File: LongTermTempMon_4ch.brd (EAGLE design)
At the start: 58.4 x 53.3 mm, 26 parts, among them IC2 LTC2418

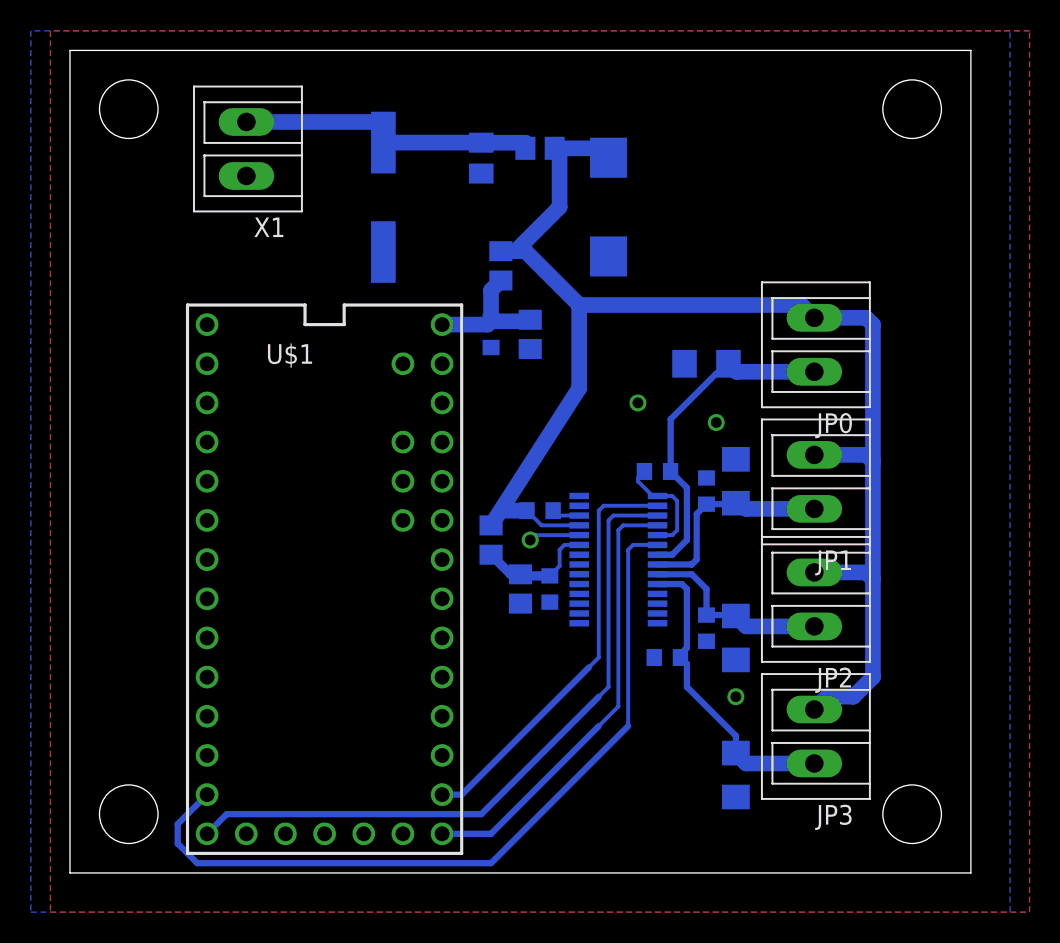
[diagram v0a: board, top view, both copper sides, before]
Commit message: Modified circuit to have reference resistor tied to +5V instead of Gnd
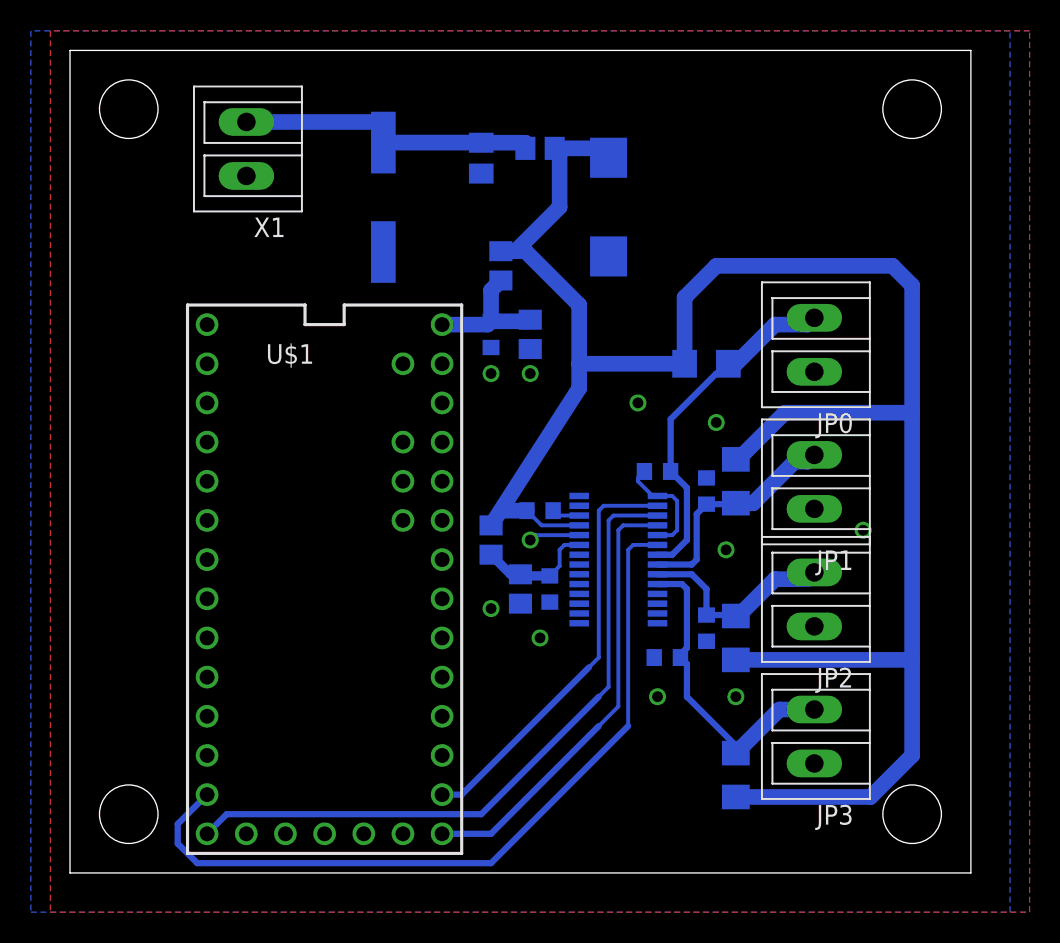
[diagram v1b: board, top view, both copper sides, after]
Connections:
- net GND: now also JP0.1, JP1.1, JP2.1, JP3.1; no longer R0.1, R1.1, R2.1, R3.1
- net IN0: now also JP0.2; no longer JP0.1
- net IN1: now also JP1.2; no longer JP1.1
- net IN2: now also JP2.2; no longer JP2.1
- net IN3: now also JP3.2; no longer JP3.1
- net VDD: now also R0.1, R1.1, R2.1, R3.1; no longer JP0.2, JP1.2, JP2.2, JP3.2
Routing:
- net VDD: track 100.0 -> 139.4 mm
- net IN1: track 13.6 -> 14.8 mm
- net IN0: track 22.4 -> 23.4 mm
- net IN2: track 12.6 -> 13.5 mm
- net IN3: track 19.7 -> 20.6 mm
- net GND: vias 4 -> 11
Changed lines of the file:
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@@
 <contactref element="IC2" pad="11"/>
 <contactref element="C10" pad="2"/>
-<contactref element="JP0" pad="2"/>
-<contactref element="JP1" pad="2"/>
-<contactref element="JP2" pad="2"/>
-<contactref element="JP3" pad="2"/>
 <wire x1="31.43" y1="46.99" x2="35.56" y2="46.99" width="1.016" layer="16"/>
 <wire x1="35.56" y1="46.99" x2="35.56" y2="45.72" width="1.016" layer="16"/>
@@
 <wire x1="27.94" y1="40.32" x2="29.53" y2="40.32" width="1.016" layer="16"/>
 <wire x1="29.53" y1="40.32" x2="33.02" y2="36.83" width="1.016" layer="16"/>
-<wire x1="33.02" y1="36.83" x2="47.44" y2="36.83" width="1.016" layer="16"/>
-<wire x1="47.44" y1="36.83" x2="48.27" y2="36" width="1.016" layer="16"/>
-<wire x1="48.27" y1="36" x2="51.63" y2="36" width="1.016" layer="16"/>
-<wire x1="51.63" y1="36" x2="52.07" y2="35.56" width="1.016" layer="16"/>
-<wire x1="52.07" y1="35.56" x2="52.07" y2="26.67" width="1.016" layer="16"/>
-<wire x1="52.07" y1="26.67" x2="52.07" y2="19.05" width="1.016" layer="16"/>
-<wire x1="52.07" y1="19.05" x2="52.07" y2="12.7" width="1.016" layer="16"/>
-<wire x1="52.07" y1="12.7" x2="50.8" y2="11.43" width="1.016" layer="16"/>
-<wire x1="50.8" y1="11.43" x2="49.1" y2="11.43" width="1.016" layer="16"/>
-<wire x1="49.1" y1="11.43" x2="48.27" y2="10.6" width="1.016" layer="16"/>
-<wire x1="48.27" y1="19.49" x2="51.63" y2="19.49" width="1.016" layer="16"/>
-<wire x1="51.63" y1="19.49" x2="52.07" y2="19.05" width="1.016" layer="16"/>
-<wire x1="48.27" y1="27.11" x2="51.63" y2="27.11" width="1.016" layer="16"/>
-<wire x1="51.63" y1="27.11" x2="52.07" y2="26.67" width="1.016" layer="16"/>
-<wire x1="33.02" y1="36.83" x2="33.02" y2="31.43" width="1.016" layer="16"/>
+<wire x1="33.02" y1="36.83" x2="33.02" y2="33.02" width="1.016" layer="16"/>
+<wire x1="33.02" y1="33.02" x2="33.02" y2="31.43" width="1.016" layer="16"/>
 <wire x1="33.02" y1="31.43" x2="27.305" y2="22.54" width="1.016" layer="16"/>
 <wire x1="33.02" y1="22.5425" x2="30.5825" y2="22.5425" width="0.254" layer="16"/>
@@
 <wire x1="27.305" y1="22.54" x2="27.305" y2="22.654421875" width="0.254" layer="16"/>
 <wire x1="27.305" y1="22.654421875" x2="28.145578125" y2="23.495" width="0.254" layer="16"/>
+<contactref element="R0" pad="1"/>
+<contactref element="R1" pad="1"/>
+<contactref element="R2" pad="1"/>
+<contactref element="R3" pad="1"/>
+<wire x1="39.853" y1="33.02" x2="33.02" y2="33.02" width="1.016" layer="16"/>
+<wire x1="39.853" y1="33.02" x2="39.853" y2="37.313" width="1.016" layer="16"/>
+<wire x1="39.853" y1="37.313" x2="41.91" y2="39.37" width="1.016" layer="16"/>
+<wire x1="41.91" y1="39.37" x2="53.34" y2="39.37" width="1.016" layer="16"/>
+<wire x1="53.34" y1="39.37" x2="54.61" y2="38.1" width="1.016" layer="16"/>
+<wire x1="43.18" y1="4.928" x2="51.918" y2="4.928" width="1.016" layer="16"/>
+<wire x1="51.918" y1="4.928" x2="54.61" y2="7.62" width="1.016" layer="16"/>
+<wire x1="54.61" y1="7.62" x2="54.61" y2="13.97" width="1.016" layer="16"/>
+<wire x1="54.61" y1="13.97" x2="54.61" y2="29.845" width="1.016" layer="16"/>
+<wire x1="54.61" y1="29.845" x2="54.61" y2="38.1" width="1.016" layer="16"/>
+<wire x1="43.18" y1="13.818" x2="54.458" y2="13.818" width="1.016" layer="16"/>
+<wire x1="54.458" y1="13.818" x2="54.61" y2="13.97" width="1.016" layer="16"/>
+<wire x1="43.18" y1="26.822" x2="43.332" y2="26.822" width="1.016" layer="16"/>
+<wire x1="43.332" y1="26.822" x2="46.355" y2="29.845" width="1.016" layer="16"/>
+<wire x1="46.355" y1="29.845" x2="54.61" y2="29.845" width="1.016" layer="16"/>
 </signal>
 <signal name="N$25">
@@
 <contactref element="U$1" pad="GND1"/>
 <contactref element="U$1" pad="AGND"/>
-<contactref element="R0" pad="1"/>
 <polygon width="0.4064" layer="16" isolate="0.6096">
 <vertex x="-2.54" y="54.61"/>
@@
 <contactref element="C10" pad="1"/>
 <contactref element="C0" pad="1"/>
-<contactref element="R1" pad="1"/>
-<contactref element="R2" pad="1"/>
-<contactref element="R3" pad="1"/>
 <contactref element="C1" pad="1"/>
 <contactref element="C2" pad="1"/>
@@
 <wire x1="30.1625" y1="21.9075" x2="29.845" y2="21.59" width="0.254" layer="16"/>
 <via x="29.845" y="21.59" extent="1-16" drill="0.7"/>
+<contactref element="JP0" pad="1"/>
+<contactref element="JP1" pad="1"/>
+<contactref element="JP2" pad="1"/>
+<contactref element="JP3" pad="1"/>
+<via x="38.1" y="11.43" extent="1-16" drill="0.7"/>
+<via x="30.48" y="15.24" extent="1-16" drill="0.7"/>
+<via x="27.305" y="17.145" extent="1-16" drill="0.7"/>
+<via x="27.305" y="32.385" extent="1-16" drill="0.7"/>
+<via x="29.845" y="32.385" extent="1-16" drill="0.7"/>
+<via x="42.545" y="20.955" extent="1-16" drill="0.7"/>
+<via x="51.435" y="22.225" extent="1-16" drill="0.7"/>
 </signal>
 <signal name="+5V">
@@
 <contactref element="IC2" pad="21"/>
 <contactref element="C0" pad="2"/>
-<contactref element="JP0" pad="1"/>
 <contactref element="R0" pad="2"/>
-<wire x1="48.27" y1="32.5" x2="43.217" y2="32.5" width="1.016" layer="16"/>
-<wire x1="43.217" y1="32.5" x2="42.697" y2="33.02" width="1.016" layer="16"/>
 <wire x1="38.1" y1="20.6375" x2="39.0525" y2="20.6375" width="0.4064" layer="16"/>
 <wire x1="39.0525" y1="20.6375" x2="40.005" y2="21.59" width="0.4064" layer="16"/>
@@
 <wire x1="41.91" y1="32.385" x2="43.028" y2="32.385" width="0.4064" layer="16"/>
 <wire x1="43.028" y1="32.385" x2="42.697" y2="33.02" width="0.4064" layer="16"/>
+<contactref element="JP0" pad="2"/>
+<wire x1="42.697" y1="33.02" x2="43.18" y2="33.02" width="1.016" layer="16"/>
+<wire x1="43.18" y1="33.02" x2="45.72" y2="35.56" width="1.016" layer="16"/>
+<wire x1="45.72" y1="35.56" x2="47.83" y2="35.56" width="1.016" layer="16"/>
+<wire x1="47.83" y1="35.56" x2="48.27" y2="36" width="1.016" layer="16"/>
 </signal>
 <signal name="IN1">
-<contactref element="JP1" pad="1"/>
 <contactref element="R1" pad="2"/>
 <contactref element="IC2" pad="22"/>
 <contactref element="C1" pad="2"/>
-<wire x1="48.27" y1="23.61" x2="43.852" y2="23.61" width="1.016" layer="16"/>
-<wire x1="43.852" y1="23.61" x2="43.18" y2="23.978" width="1.016" layer="16"/>
 <wire x1="38.1" y1="20.0025" x2="40.3225" y2="20.0025" width="0.4064" layer="16"/>
 <wire x1="40.3225" y1="20.0025" x2="40.64" y2="20.32" width="0.4064" layer="16"/>
@@
 <wire x1="41.275" y1="23.915" x2="42.813" y2="23.915" width="0.4064" layer="16"/>
 <wire x1="42.813" y1="23.915" x2="43.18" y2="23.978" width="0.4064" layer="16"/>
+<contactref element="JP1" pad="2"/>
+<wire x1="43.18" y1="23.978" x2="44.298" y2="23.978" width="1.016" layer="16"/>
+<wire x1="44.298" y1="23.978" x2="46.99" y2="26.67" width="1.016" layer="16"/>
+<wire x1="46.99" y1="26.67" x2="47.83" y2="26.67" width="1.016" layer="16"/>
+<wire x1="47.83" y1="26.67" x2="48.27" y2="27.11" width="1.016" layer="16"/>
 </signal>
 <signal name="IN2">
-<contactref element="JP2" pad="1"/>
 <contactref element="R2" pad="2"/>
 <contactref element="IC2" pad="23"/>
 <contactref element="C2" pad="2"/>
-<wire x1="48.27" y1="15.99" x2="43.852" y2="15.99" width="1.016" layer="16"/>
-<wire x1="43.852" y1="15.99" x2="43.18" y2="16.662" width="1.016" layer="16"/>
 <wire x1="38.1" y1="19.3675" x2="40.3225" y2="19.3675" width="0.4064" layer="16"/>
 <wire x1="40.3225" y1="19.3675" x2="41.275" y2="18.415" width="0.4064" layer="16"/>
@@
 <wire x1="41.275" y1="16.725" x2="43.117" y2="16.725" width="0.4064" layer="16"/>
 <wire x1="43.117" y1="16.725" x2="43.18" y2="16.662" width="0.4064" layer="16"/>
+<contactref element="JP2" pad="2"/>
+<wire x1="43.18" y1="16.662" x2="43.332" y2="16.662" width="1.016" layer="16"/>
+<wire x1="43.332" y1="16.662" x2="45.72" y2="19.05" width="1.016" layer="16"/>
+<wire x1="45.72" y1="19.05" x2="47.83" y2="19.05" width="1.016" layer="16"/>
+<wire x1="47.83" y1="19.05" x2="48.27" y2="19.49" width="1.016" layer="16"/>
 </signal>
 <signal name="IN3">
-<contactref element="JP3" pad="1"/>
 <contactref element="R3" pad="2"/>
 <contactref element="IC2" pad="24"/>
 <contactref element="C3" pad="2"/>
-<wire x1="48.27" y1="7.1" x2="43.852" y2="7.1" width="1.016" layer="16"/>
-<wire x1="43.852" y1="7.1" x2="43.18" y2="7.772" width="1.016" layer="16"/>
-<wire x1="43.18" y1="7.772" x2="43.18" y2="8.89" width="0.4064" layer="16"/>
-<wire x1="43.18" y1="8.89" x2="40.005" y2="12.065" width="0.4064" layer="16"/>
 <wire x1="38.1" y1="18.7325" x2="39.6875" y2="18.7325" width="0.4064" layer="16"/>
 <wire x1="39.6875" y1="18.7325" x2="40.005" y2="18.415" width="0.4064" layer="16"/>
 <wire x1="40.005" y1="18.415" x2="40.005" y2="14.605" width="0.4064" layer="16"/>
-<wire x1="40.005" y1="12.065" x2="40.005" y2="13.55" width="0.4064" layer="16"/>
-<wire x1="40.005" y1="13.55" x2="39.585" y2="13.97" width="0.4064" layer="16"/>
 <wire x1="39.585" y1="13.97" x2="39.585" y2="14.185" width="0.4064" layer="16"/>
 <wire x1="39.585" y1="14.185" x2="40.005" y2="14.605" width="0.4064" layer="16"/>
+<contactref element="JP3" pad="2"/>
+<wire x1="48.27" y1="10.6" x2="46.008" y2="10.6" width="1.016" layer="16"/>
+<wire x1="46.008" y1="10.6" x2="43.18" y2="7.772" width="1.016" layer="16"/>
+<wire x1="43.18" y1="7.772" x2="43.18" y2="8.255" width="0.4064" layer="16"/>
+<wire x1="43.18" y1="8.255" x2="40.005" y2="11.43" width="0.4064" layer="16"/>
+<wire x1="40.005" y1="11.43" x2="40.005" y2="13.55" width="0.4064" layer="16"/>
+<wire x1="40.005" y1="13.55" x2="39.585" y2="13.97" width="0.4064" layer="16"/>
 </signal>
 </signals>
